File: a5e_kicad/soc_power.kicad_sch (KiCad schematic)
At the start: 70 parts, among them U7 A5EB013B-B23B

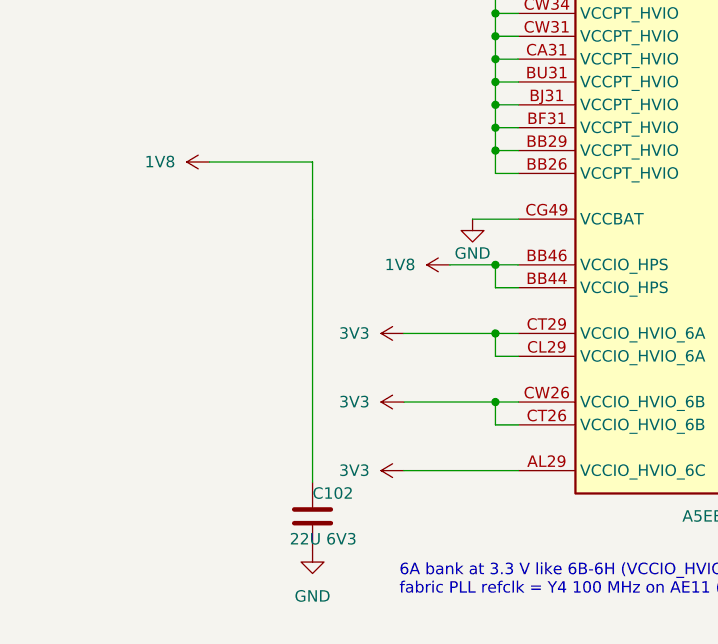
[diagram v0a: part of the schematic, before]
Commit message: Ethernet PHY passives to 0201, R27/R28 to 0402, preliminary RGMII routing
- 31 PHY passives on the hps_ethernet sheet 0402 -> 0201 (C24 22u stays
  0402): 100n C190183, 1u C272877, 27p C85899, 10k C473048,
  330R C516485, 4K7 C270346, 1K5 C270361, 2K49 C473476.
- Refclk bias R27/R28 0201 -> 0402 (C25120, 49.9R); R28 moved 0.1 mm
  to +x to clear the refclk_N meander.
- Preliminary RGMII routing: RX on F.Cu, TX on In2. Group spread
  TX 79 ps (TXD1 longest), RX 44 ps.
- Schematic sheets as saved by eeschema.
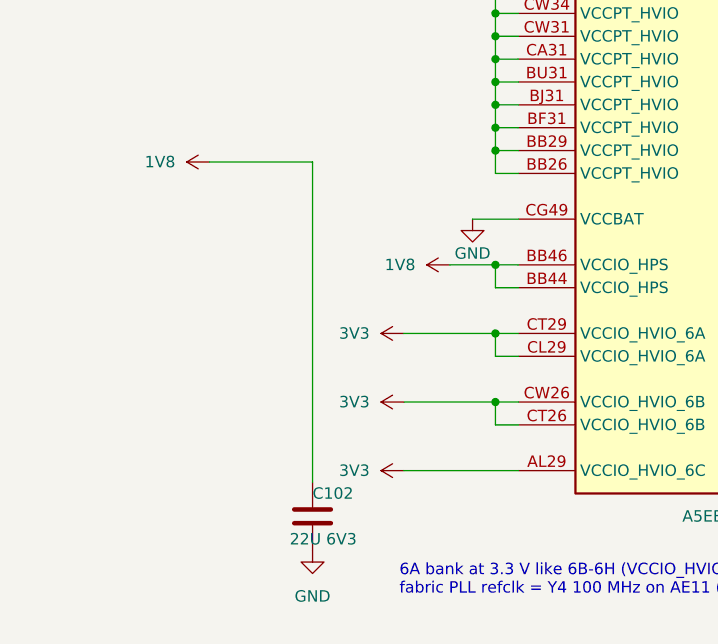
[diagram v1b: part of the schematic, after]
